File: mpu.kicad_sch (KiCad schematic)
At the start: 14 parts, among them IC19 MC6809E, SW1 RESET

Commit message: move to samx4
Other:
- company: (none) -> Dragon Data
- title: (none) -> Dragon 32 CPU UK PAL
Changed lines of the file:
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@@
   (paper "A3")
   (title_block
+    (title "Dragon 32 CPU UK PAL")
     (date "2023-05-25")
     (rev "3.0")
-    (comment 2 "Reposition dram and buffer")
+    (company "Dragon Data")
+    (comment 1 "Modified by Julian Brown")
+    (comment 2 "SAMx4 by Ciaran Anscomb")
   )
   (junction (at 137.668 106.934) (diameter 0) (color 0 0 0 0)

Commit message: rework board
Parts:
- C22: footprint Capacitor_THT:CP_Radial_D6.3mm_P2.50mm -> Capacitor_SMD:CP_Elec_5x5.3
- C23: footprint Capacitor_THT:CP_Radial_D5.0mm_P2.50mm -> Capacitor_SMD:CP_Elec_4x4.5; DigiKey 732-8966-1-ND -> 732-8541-1-ND
- C4: footprint Capacitor_THT:C_Disc_D4.3mm_W1.9mm_P5.00mm -> Capacitor_SMD:C_0805_2012Metric_Pad1.18x1.45mm_HandSolder
- D4, D5, D6: footprint Diode_THT:D_DO-35_SOD27_P2.54mm_Vertical_KathodeUp -> Diode_SMD:D_SOD-323_HandSoldering
- R13, R14, R15, R36, R40, R41: footprint Resistor_THT:R_Axial_DIN0207_L6.3mm_D2.5mm_P2.54mm_Vertical -> Resistor_SMD:R_0805_2012Metric_Pad1.20x1.40mm_HandSolder
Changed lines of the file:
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@@
       (effects (font (size 1.27 1.27)))
     )
-    (property "Footprint" "Diode_THT:D_DO-35_SOD27_P2.54mm_Vertical_KathodeUp" (at 86.233 91.694 0)
+    (property "Footprint" "Diode_SMD:D_SOD-323_HandSoldering" (at 86.233 91.694 0)
       (effects (font (size 1.27 1.27)) hide)
     )
@@
       (effects (font (size 1.27 1.27)))
     )
-    (property "Footprint" "Capacitor_THT:CP_Radial_D6.3mm_P2.50mm" (at 173.863 58.674 0)
+    (property "Footprint" "Capacitor_SMD:CP_Elec_5x5.3" (at 173.863 58.674 0)
       (effects (font (size 1.27 1.27)) hide)
     )
@@
       (effects (font (size 1.27 1.27)) (justify left))
     )
-    (property "Footprint" "Resistor_THT:R_Axial_DIN0207_L6.3mm_D2.5mm_P2.54mm_Vertical" (at 137.668 104.394 0)
+    (property "Footprint" "Resistor_SMD:R_0805_2012Metric_Pad1.20x1.40mm_HandSolder" (at 137.668 104.394 0)
       (effects (font (size 1.27 1.27)) hide)
     )
@@
       (effects (font (size 1.27 1.27)) (justify left))
     )
-    (property "Footprint" "Resistor_THT:R_Axial_DIN0207_L6.3mm_D2.5mm_P2.54mm_Vertical" (at 121.412 81.534 90)
+    (property "Footprint" "Resistor_SMD:R_0805_2012Metric_Pad1.20x1.40mm_HandSolder" (at 121.412 81.534 90)
       (effects (font (size 1.27 1.27)) hide)
     )
@@
       (effects (font (size 1.27 1.27)) (justify left))
     )
-    (property "Footprint" "Resistor_THT:R_Axial_DIN0207_L6.3mm_D2.5mm_P2.54mm_Vertical" (at 100.33 91.694 90)
+    (property "Footprint" "Resistor_SMD:R_0805_2012Metric_Pad1.20x1.40mm_HandSolder" (at 100.33 91.694 90)
       (effects (font (size 1.27 1.27)) hide)
     )
@@
       (effects (font (size 1.27 1.27)))
     )
-    (property "Footprint" "Diode_THT:D_DO-35_SOD27_P2.54mm_Vertical_KathodeUp" (at 84.963 91.694 0)
+    (property "Footprint" "Diode_SMD:D_SOD-323_HandSoldering" (at 84.963 91.694 0)
       (effects (font (size 1.27 1.27)) hide)
     )
@@
       (effects (font (size 1.27 1.27)))
     )
-    (property "Footprint" "Diode_THT:D_DO-35_SOD27_P2.54mm_Vertical_KathodeUp" (at 76.073 101.854 0)
+    (property "Footprint" "Diode_SMD:D_SOD-323_HandSoldering" (at 76.073 101.854 0)
       (effects (font (size 1.27 1.27)) hide)
     )
@@
       (effects (font (size 1.27 1.27)) (justify left))
     )
-    (property "Footprint" "Resistor_THT:R_Axial_DIN0207_L6.3mm_D2.5mm_P2.54mm_Vertical" (at 144.653 98.425 0)
+    (property "Footprint" "Resistor_SMD:R_0805_2012Metric_Pad1.20x1.40mm_HandSolder" (at 144.653 98.425 0)
       (effects (font (size 1.27 1.27)) hide)
     )
@@
       (effects (font (size 1.27 1.27)) (justify left))
     )
-    (property "Footprint" "Capacitor_THT:C_Disc_D4.3mm_W1.9mm_P5.00mm" (at 90.678 101.854 0)
+    (property "Footprint" "Capacitor_SMD:C_0805_2012Metric_Pad1.18x1.45mm_HandSolder" (at 90.678 101.854 0)
       (effects (font (size 1.27 1.27)) hide)
     )
@@
       (effects (font (size 1.27 1.27)) (justify left))
     )
-    (property "Footprint" "Resistor_THT:R_Axial_DIN0207_L6.3mm_D2.5mm_P2.54mm_Vertical" (at 151.511 98.425 0)
+    (property "Footprint" "Resistor_SMD:R_0805_2012Metric_Pad1.20x1.40mm_HandSolder" (at 151.511 98.425 0)
       (effects (font (size 1.27 1.27)) hide)
     )
@@
       (effects (font (size 1.27 1.27)) (justify left))
     )
-    (property "Footprint" "Resistor_THT:R_Axial_DIN0207_L6.3mm_D2.5mm_P2.54mm_Vertical" (at 137.668 98.425 0)
+    (property "Footprint" "Resistor_SMD:R_0805_2012Metric_Pad1.20x1.40mm_HandSolder" (at 137.668 98.425 0)
       (effects (font (size 1.27 1.27)) hide)
     )
@@
       (effects (font (size 1.27 1.27)) (justify left))
     )
-    (property "Footprint" "Capacitor_THT:CP_Radial_D5.0mm_P2.50mm" (at 123.19 92.964 0)
+    (property "Footprint" "Capacitor_SMD:CP_Elec_4x4.5" (at 123.19 92.964 0)
       (effects (font (size 1.27 1.27)) hide)
     )
@@
       (effects (font (size 1.27 1.27)) hide)
     )
-    (property "DigiKey" "732-8966-1-ND" (at 123.19 92.964 0)
-      (effects (font (size 1.27 1.27)) hide)
-    )
+    (property "DigiKey" "732-8541-1-ND" (at 123.19 92.964 0)
+      (effects (font (size 1.27 1.27)) hide)
+    )

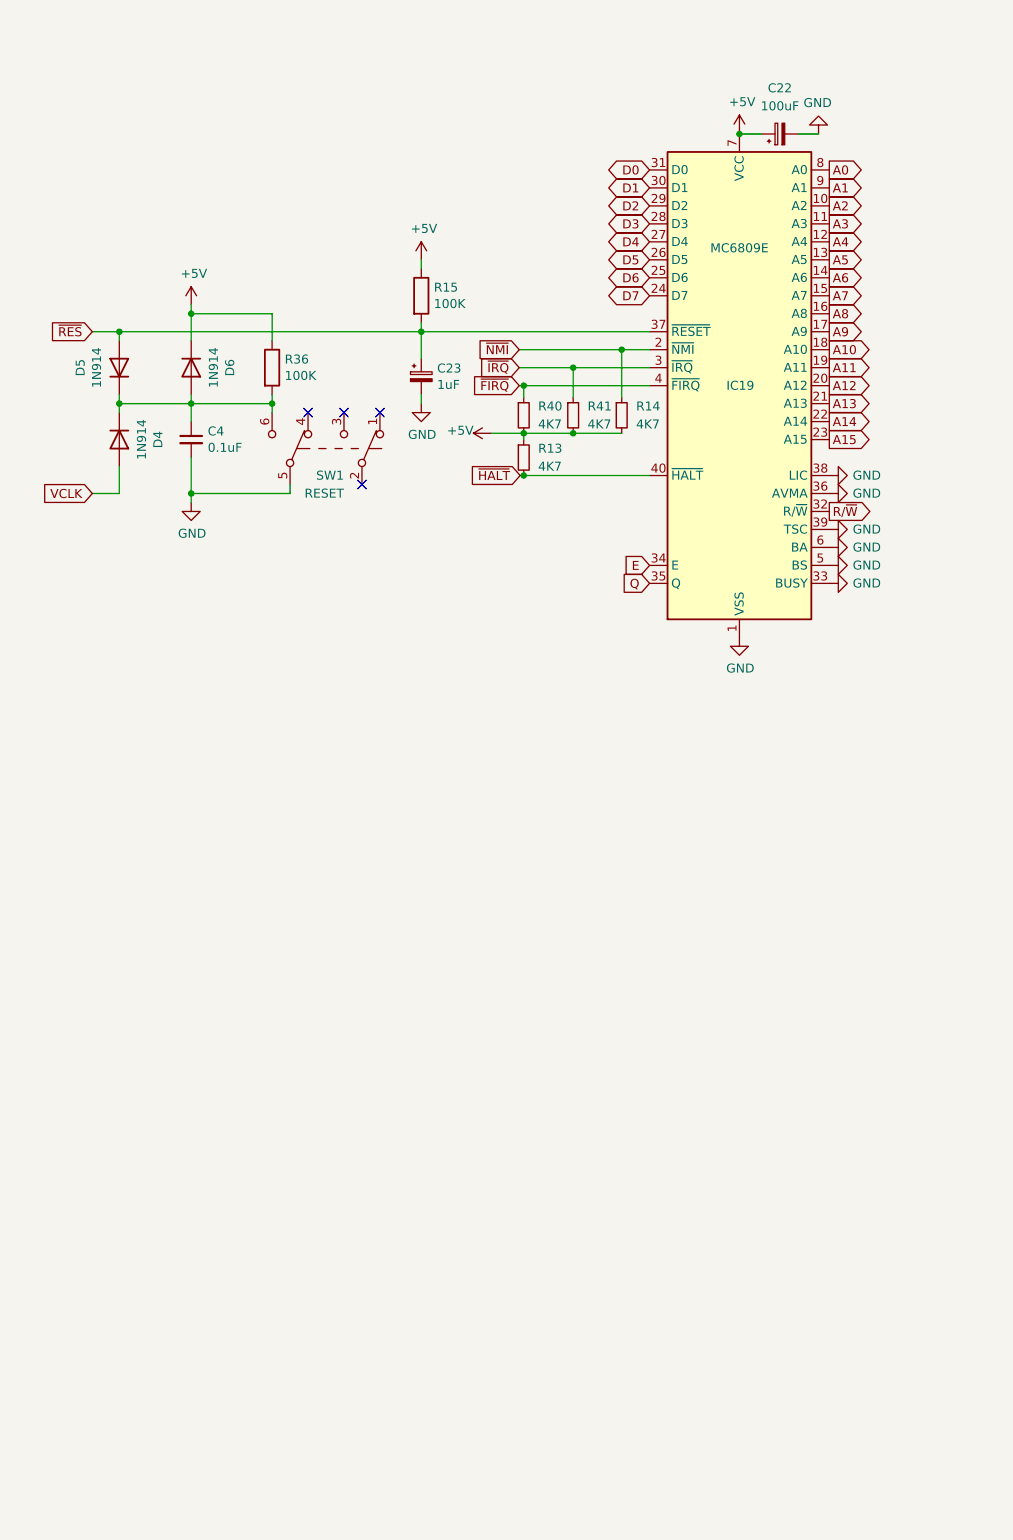
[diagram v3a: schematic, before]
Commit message: switch to fpga
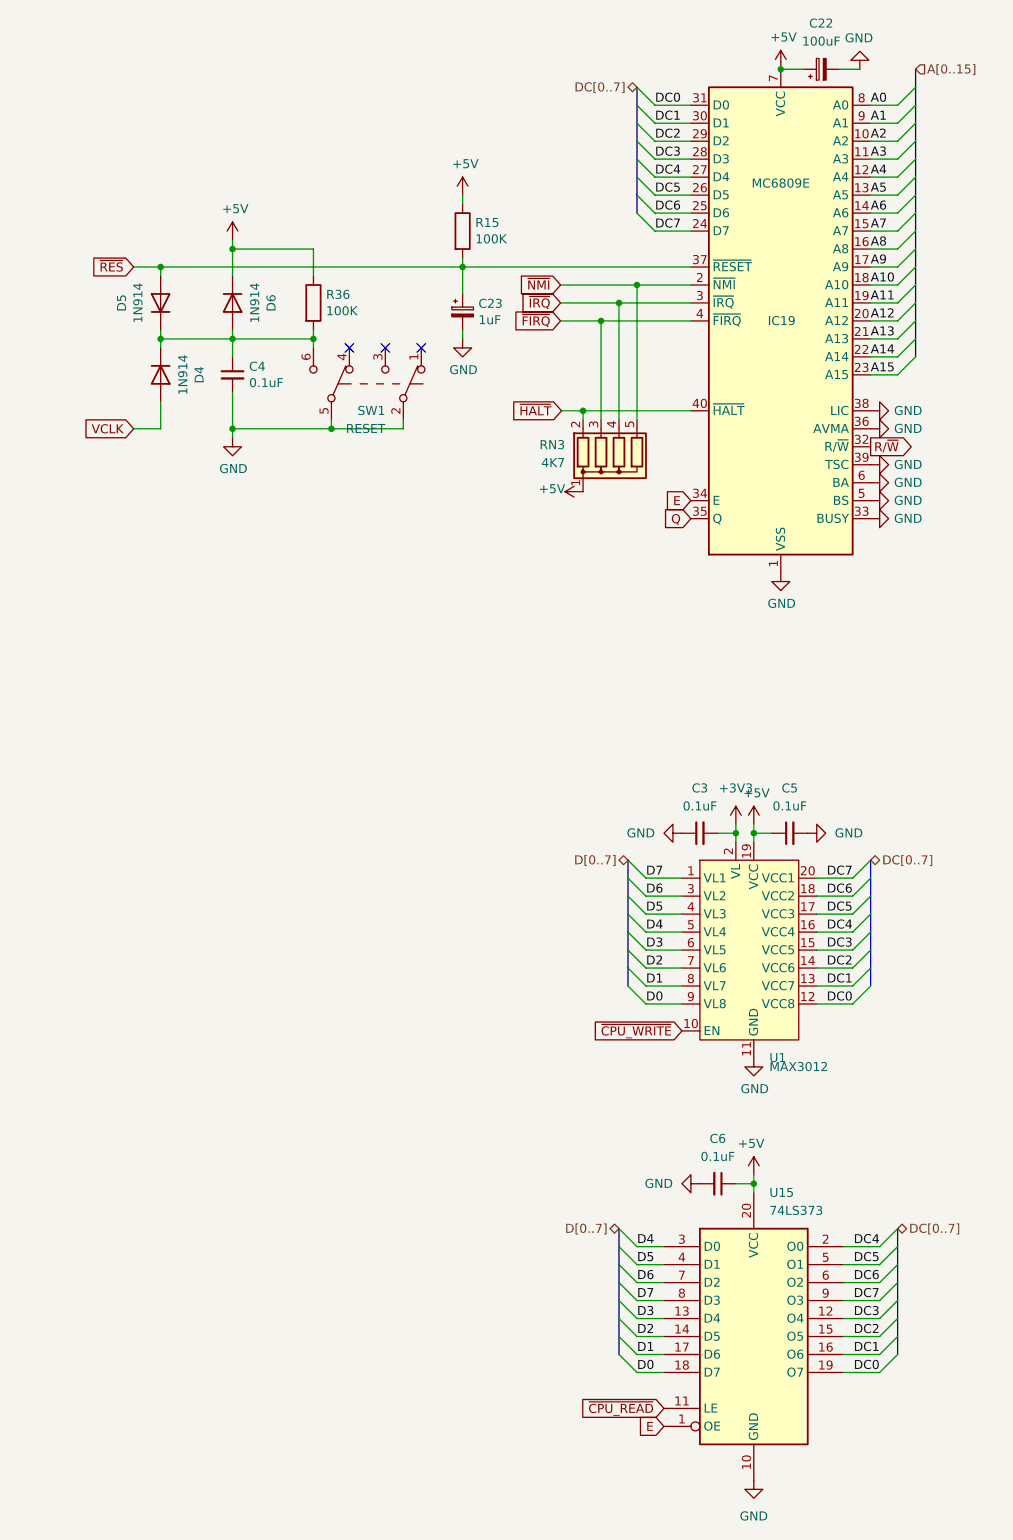
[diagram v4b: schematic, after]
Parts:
- removed R13, R14, R40, R41: 4K7, Resistor_SMD:R_0805_2012Metric_Pad1.20x1.40mm_HandSolder, symbol Device:R_Small
- added C3, C5, C6: 0.1uF, Capacitor_SMD:C_0805_2012Metric_Pad1.18x1.45mm_HandSolder, symbol Device:C_Small
- added RN3: 4K7, Resistor_THT:R_Array_SIP5, symbol Device:R_Network04
- added U1: MAX3012, Package_SO:TSSOP-20_4.4x6.5mm_P0.65mm, symbol Motorola PIA:MAX3012
- added U15: 74LS373, symbol 74xx:74LS373
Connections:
- net +5V: now also C5.1, C6.1, RN3.1 (common), U1.19 (VCC), U15.20 (VCC)
- net D0: now also U1.9 (VL8), U15.18 (D7); no longer IC19.31 (D0)
- net D1: now also U1.8 (VL7), U15.17 (D6); no longer IC19.30 (D1)
- net D2: now also U1.7 (VL6), U15.14 (D5); no longer IC19.29 (D2)
- net D3: now also U1.6 (VL5), U15.13 (D4); no longer IC19.28 (D3)
- net D4: now also U1.5 (VL4), U15.3 (D0); no longer IC19.27 (D4)
- net D5: now also U1.4 (VL3), U15.4 (D1); no longer IC19.26 (D5)
- net D6: now also U1.3 (VL2), U15.7 (D2); no longer IC19.25 (D6)
- net D7: now also U1.1 (VL1), U15.8 (D3); no longer IC19.24 (D7)
- net E: now also U15.1 (OE)
- net GND: now also SW1.2 (B), C3.1, C5.2, C6.2, U1.11 (GND), U15.10 (GND)
- net ~{FIRQ}: now also RN3.3 (R2)
- net ~{HALT}: now also RN3.2 (R1)
- net ~{IRQ}: now also RN3.4 (R3)
- net ~{NMI}: now also RN3.5 (R4)
- new net +3V3: C3.2, U1.2 (VL)
- new net DC0: IC19.31 (D0), U1.12 (VCC8), U15.19 (O7)
- new net DC1: IC19.30 (D1), U1.13 (VCC7), U15.16 (O6)
- new net DC2: IC19.29 (D2), U1.14 (VCC6), U15.15 (O5)
- new net DC3: IC19.28 (D3), U1.15 (VCC5), U15.12 (O4)
- new net DC4: IC19.27 (D4), U1.16 (VCC4), U15.2 (O0)
- new net DC5: IC19.26 (D5), U1.17 (VCC3), U15.5 (O1)
- new net DC6: IC19.25 (D6), U1.18 (VCC2), U15.6 (O2)
- new net DC7: IC19.24 (D7), U1.20 (VCC1), U15.9 (O3)
- new net ~{CPU_READ}: U15.11 (LE)
- new net ~{CPU_WRITE}: U1.10 (EN)
- no-connect marks 4 -> 3
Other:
- moved on the sheet: C22, C23, C4, D4, D5, D6, IC19, R15, R36, SW1

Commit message: rework traces for FPGA
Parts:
- U15: footprint (none) -> Package_SO:SOIC-20W_7.5x12.8mm_P1.27mm
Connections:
- net D0: now also U15.3 (D0); no longer U15.18 (D7)
- net D1: now also U15.4 (D1); no longer U15.17 (D6)
- net D2: now also U15.7 (D2); no longer U15.14 (D5)
- net D3: now also U15.8 (D3); no longer U15.13 (D4)
- net D4: now also U15.18 (D7); no longer U15.3 (D0)
- net D5: now also U15.17 (D6); no longer U15.4 (D1)
- net D6: now also U15.14 (D5); no longer U15.7 (D2)
- net D7: now also U15.13 (D4); no longer U15.8 (D3)
- net DC0: now also U15.2 (O0); no longer U15.19 (O7)
- net DC1: now also U15.5 (O1); no longer U15.16 (O6)
- net DC2: now also U15.6 (O2); no longer U15.15 (O5)
- net DC3: now also U15.9 (O3); no longer U15.12 (O4)
- net DC4: now also U15.19 (O7); no longer U15.2 (O0)
- net DC5: now also U15.16 (O6); no longer U15.5 (O1)
- net DC6: now also U15.15 (O5); no longer U15.6 (O2)
- net DC7: now also U15.12 (O4); no longer U15.9 (O3)
- net E: no longer U15.1 (OE)
- net ~{CPU_READ} renamed CPU_READ
- net ~{CPU_WRITE} renamed CPU_WRITE
- new net ~{E}: U15.1 (OE)
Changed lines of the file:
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@@
 	)
 	(label "D3"
-		(at 153.67 226.06 0)
+		(at 153.67 223.52 0)
 		(fields_autoplaced yes)
 		(effects
@@
 	)
 	(label "DC4"
-		(at 187.96 215.9 180)
+		(at 187.96 233.68 180)
 		(fields_autoplaced yes)
 		(effects
@@
 	)
 	(label "D4"
-		(at 153.67 215.9 0)
+		(at 153.67 233.68 0)
 		(fields_autoplaced yes)
 		(effects
@@
 	)
 	(label "DC0"
-		(at 187.96 233.68 180)
+		(at 187.96 215.9 180)
 		(fields_autoplaced yes)
 		(effects
@@
 	)
 	(label "DC6"
-		(at 187.96 220.98 180)
+		(at 187.96 228.6 180)
 		(fields_autoplaced yes)
 		(effects
@@
 	)
 	(label "D6"
-		(at 153.67 220.98 0)
+		(at 153.67 228.6 0)
 		(fields_autoplaced yes)
 		(effects
@@
 	)
 	(label "DC7"
+		(at 187.96 226.06 180)
+		(fields_autoplaced yes)
+		(effects
+			(font
+				(size 1.27 1.27)
+			)
+			(justify right bottom)
+		)
+	)
+	(label "DC3"
 		(at 187.96 223.52 180)
-		(fields_autoplaced yes)
-		(effects
-			(font
-				(size 1.27 1.27)
-			)
-			(justify right bottom)
-		)
-	)
-	(label "DC3"
-		(at 187.96 226.06 180)
 		(fields_autoplaced yes)
 		(effects
@@
 	)
 	(label "D1"
-		(at 153.67 231.14 0)
+		(at 153.67 218.44 0)
 		(fields_autoplaced yes)
 		(effects
@@
 	)
 	(label "D7"
-		(at 153.67 223.52 0)
+		(at 153.67 226.06 0)
 		(fields_autoplaced yes)
 		(effects
@@
 	)
 	(label "D5"
-		(at 153.67 218.44 0)
+		(at 153.67 231.14 0)
 		(fields_autoplaced yes)
 		(effects
@@
 	)
 	(label "DC5"
-		(at 187.96 218.44 180)
+		(at 187.96 231.14 180)
 		(fields_autoplaced yes)
 		(effects
@@
 	)
 	(label "D2"
-		(at 153.67 228.6 0)
+		(at 153.67 220.98 0)
 		(fields_autoplaced yes)
 		(effects
@@
 	)
 	(label "DC2"
-		(at 187.96 228.6 180)
+		(at 187.96 220.98 180)
 		(fields_autoplaced yes)
 		(effects
@@
 	)
 	(label "DC1"
-		(at 187.96 231.14 180)
+		(at 187.96 218.44 180)
 		(fields_autoplaced yes)
 		(effects
@@
 	)
 	(label "D0"
-		(at 153.67 233.68 0)
+		(at 153.67 215.9 0)
 		(fields_autoplaced yes)
 		(effects
@@
 		)
 	)
-	(global_label "E"
+	(global_label "~{E}"
 		(shape input)
 		(at 157.48 241.3 180)
@@
 		)
 		(property "Intersheetrefs" "${INTERSHEET_REFS}"
-			(at 154.0068 241.2206 0)
+			(at 154 241.3 0)
 			(effects
 				(font
@@
 		)
 	)
-	(global_label "~{CPU_READ}"
+	(global_label "CPU_READ"
 		(shape input)
 		(at 157.48 238.76 180)
@@
 		)
 		(property "Intersheetrefs" "${INTERSHEET_REFS}"
-			(at 144.8791 238.76 0)
+			(at 145.5333 238.76 0)
 			(effects
 				(font
@@
 		)
 	)
-	(global_label "~{CPU_WRITE}"
+	(global_label "CPU_WRITE"
 		(shape input)
 		(at 160.02 185.42 180)
@@
 		)
 		(property "Intersheetrefs" "${INTERSHEET_REFS}"
-			(at 146.7539 185.42 0)
+			(at 147.4081 185.42 0)
 			(effects
 				(font
@@
 			)
 		)
-		(property "Footprint" ""
+		(property "Footprint" "Package_SO:SOIC-20W_7.5x12.8mm_P1.27mm"
 			(at 170.18 228.6 0)
 			(effects
